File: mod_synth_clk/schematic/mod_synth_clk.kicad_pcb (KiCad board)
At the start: 2 copper layers, 17.8 x 113 mm, 9 parts, among them J1 Clock, J2 Conn_02x08_Odd_Even

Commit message: Shorten clock PCB to 109mm
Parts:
- moved J1 3.81 mm to (40.6, 128.3)
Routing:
- net Net-(J1-PadT): track 54.6 -> 50.8 mm
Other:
- board size 17.8 x 113 mm -> 17.8 x 109.2 mm
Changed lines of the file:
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@@
   )
   (module Connector_Audio:Jack_3.5mm_QingPu_WQP-PJ398SM_Vertical_CircularHoles (layer F.Cu)
-    (at 40.64 132.08 90)
+    (at 40.64 128.27 90)
     (descr "TRS 3.5mm, vertical, Thonkiconn, PCB mount, (http://www.qingpu-electronics.com/en/products/WQP-PJ398SM-362.html)")
     (tags "WQP-PJ398SM WQP-PJ301M-12 TRS 3.5mm mono vertical jack thonkiconn qingpu")
@@
     )
   )
+  (gr_line (start 55.88 134.62) (end 55.88 25.4) (layer Edge.Cuts) (width 0.05))
+  (gr_line (start 38.1 134.62) (end 55.88 134.62) (layer Edge.Cuts) (width 0.05))
+  (gr_line (start 38.1 25.4) (end 38.1 134.62) (layer Edge.Cuts) (width 0.05))
   (gr_line (start 55.88 25.4) (end 38.1 25.4) (layer Edge.Cuts) (width 0.05))
-  (gr_line (start 55.88 138.43) (end 55.88 25.4) (layer Edge.Cuts) (width 0.05))
-  (gr_line (start 38.1 138.43) (end 55.88 138.43) (layer Edge.Cuts) (width 0.05))
-  (gr_line (start 38.1 25.4) (end 38.1 138.43) (layer Edge.Cuts) (width 0.05))
   (segment (start 48.26 83.82) (end 48.26 85.09) (width 0.25) (layer F.Cu) (net 1))
   (segment (start 48.26 85.09) (end 52.07 85.09) (width 0.25) (layer F.Cu) (net 1))
@@
   (segment (start 50.8 54.61) (end 48.26 54.61) (width 0.25) (layer F.Cu) (net 32))
   (segment (start 48.26 54.61) (end 48.26 62.23) (width 0.25) (layer F.Cu) (net 32))
-  (segment (start 52.04 132.08) (end 52.04 90.2) (width 0.25) (layer F.Cu) (net 33))
-  (segment (start 52.04 90.2) (end 52.01 90.17) (width 0.25) (layer F.Cu) (net 33))
   (segment (start 52.01 90.17) (end 44.45 90.17) (width 0.25) (layer F.Cu) (net 33))
   (segment (start 44.45 90.17) (end 44.45 85.09) (width 0.25) (layer F.Cu) (net 33))
+  (segment (start 52.04 90.2) (end 52.04 128.27) (width 0.25) (layer F.Cu) (net 33))
+  (segment (start 52.01 90.17) (end 52.04 90.2) (width 0.25) (layer F.Cu) (net 33))
   (zone (net 5) (net_name GND) (layer B.Cu) (hatch edge 0.508)
     (connect_pads (clearance 0.508))
@@
     (polygon
       (pts
-        (xy 38.1 138.43) (xy 55.88 138.43) (xy 55.88 25.4) (xy 38.1 25.4)
+        (xy 55.88 134.62) (xy 38.1 134.62) (xy 38.1 25.4) (xy 55.88 25.4)
       )
     )

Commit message: Update PCB layouts
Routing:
- net Net-(J2-Pad3): track 0.00 -> 5.08 mm
- added copper zone on F.Cu, net GND
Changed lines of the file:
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@@
     (thickness 1.6)
     (drawings 4)
-    (tracks 49)
+    (tracks 51)
     (zones 0)
     (modules 9)
@@
   (segment (start 52.04 90.2) (end 52.04 128.27) (width 0.25) (layer F.Cu) (net 33))
   (segment (start 52.01 90.17) (end 52.04 90.2) (width 0.25) (layer F.Cu) (net 33))
+  (segment (start 45.72 109.22) (end 45.72 111.76) (width 0.25) (layer B.Cu) (net 40))
+  (segment (start 45.72 114.3) (end 45.72 111.76) (width 0.25) (layer B.Cu) (net 40))
+  (zone (net 5) (net_name GND) (layer F.Cu) (hatch edge 0.508)
+    (connect_pads (clearance 0.508))
+    (min_thickness 0.254)
+    (fill yes (arc_segments 32) (thermal_gap 0.508) (thermal_bridge_width 0.508))
+    (polygon
+      (pts
+        (xy 38.1 25.4) (xy 55.88 25.4) (xy 55.88 134.62) (xy 38.1 134.62)
+      )
+    )
+  )
   (zone (net 5) (net_name GND) (layer B.Cu) (hatch edge 0.508)
     (connect_pads (clearance 0.508))
@@
     (polygon
       (pts
-        (xy 55.88 134.62) (xy 38.1 134.62) (xy 38.1 25.4) (xy 55.88 25.4)
+        (xy 38.1 25.4) (xy 55.88 25.4) (xy 55.88 134.62) (xy 38.1 134.62)
       )
     )

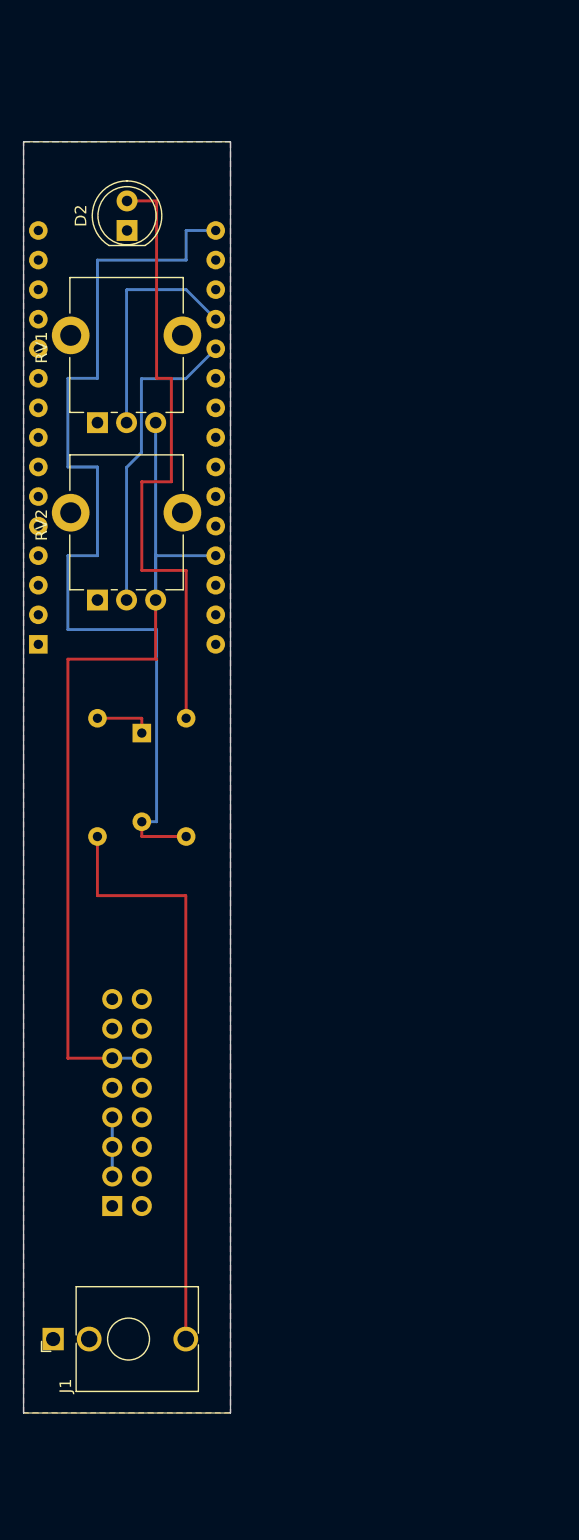
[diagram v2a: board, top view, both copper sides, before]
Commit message: Add possible PCB front panel
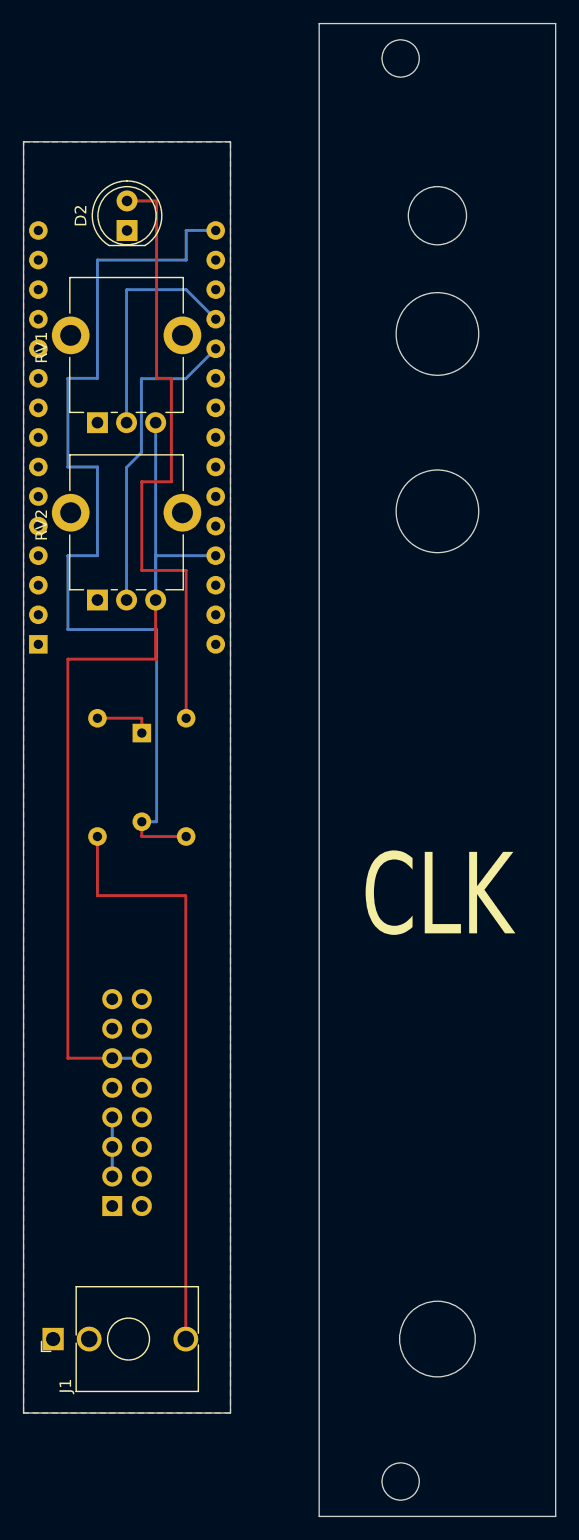
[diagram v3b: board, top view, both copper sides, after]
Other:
- board size 17.8 x 109.2 mm -> 45.7 x 128.3 mm
- board text added: "CLK"
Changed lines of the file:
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@@
   (general
     (thickness 1.6)
-    (drawings 4)
+    (drawings 15)
     (tracks 51)
     (zones 0)
@@
     )
   )
+  (gr_text CLK (at 73.66 90.17) (layer F.SilkS)
+    (effects (font (size 7 5) (thickness 1)))
+  )
+  (gr_circle (center 70.5 140.51) (end 72.1 140.51) (layer Edge.Cuts) (width 0.05))
+  (gr_circle (center 70.5 18.24) (end 72.1 18.24) (layer Edge.Cuts) (width 0.05))
+  (gr_circle (center 73.66 31.75) (end 76.16 31.75) (layer Edge.Cuts) (width 0.05))
+  (gr_circle (center 73.66 41.91) (end 77.21 41.91) (layer Edge.Cuts) (width 0.05))
+  (gr_circle (center 73.66 57.15) (end 77.21 57.15) (layer Edge.Cuts) (width 0.05))
+  (gr_circle (center 73.66 128.27) (end 76.91 128.27) (layer Edge.Cuts) (width 0.05))
+  (gr_line (start 83.82 15.24) (end 63.5 15.24) (layer Edge.Cuts) (width 0.05))
+  (gr_line (start 83.82 143.51) (end 83.82 15.24) (layer Edge.Cuts) (width 0.05))
+  (gr_line (start 63.5 143.51) (end 83.82 143.51) (layer Edge.Cuts) (width 0.05))
+  (gr_line (start 63.5 15.24) (end 63.5 143.51) (layer Edge.Cuts) (width 0.05))
   (gr_line (start 55.88 134.62) (end 55.88 25.4) (layer Edge.Cuts) (width 0.05))
   (gr_line (start 38.1 134.62) (end 55.88 134.62) (layer Edge.Cuts) (width 0.05))

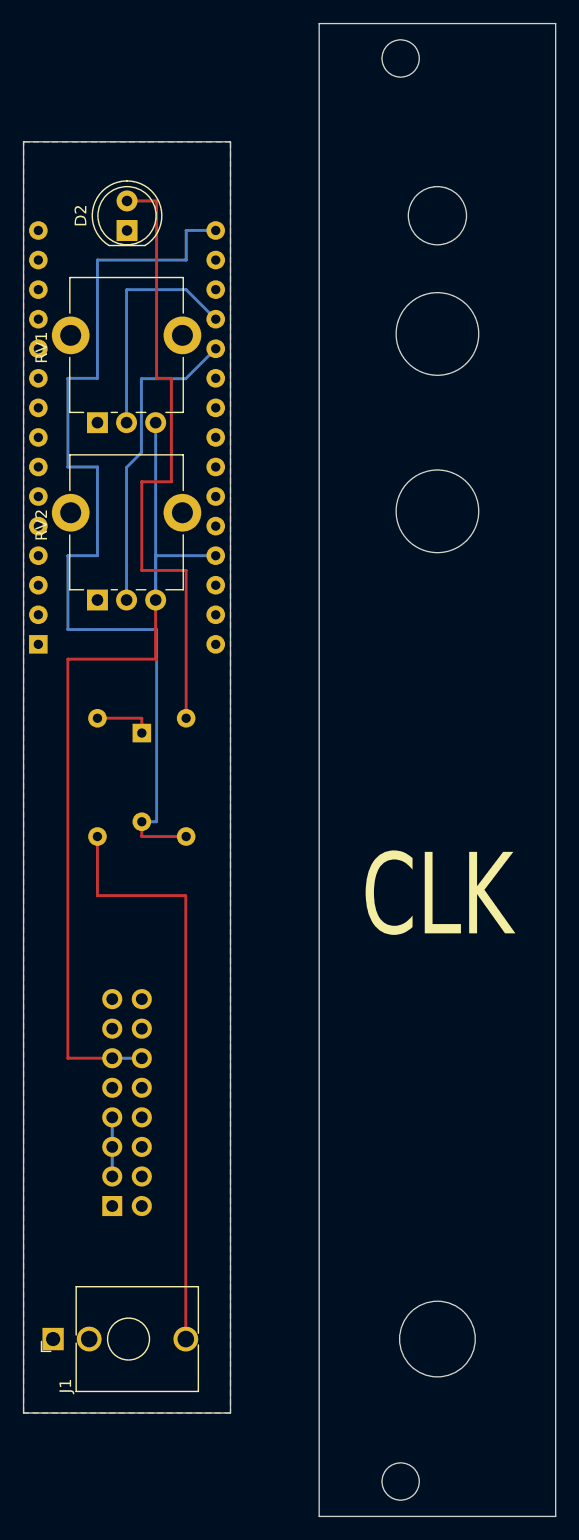
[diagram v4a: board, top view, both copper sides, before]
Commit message: Remove PCB front panel
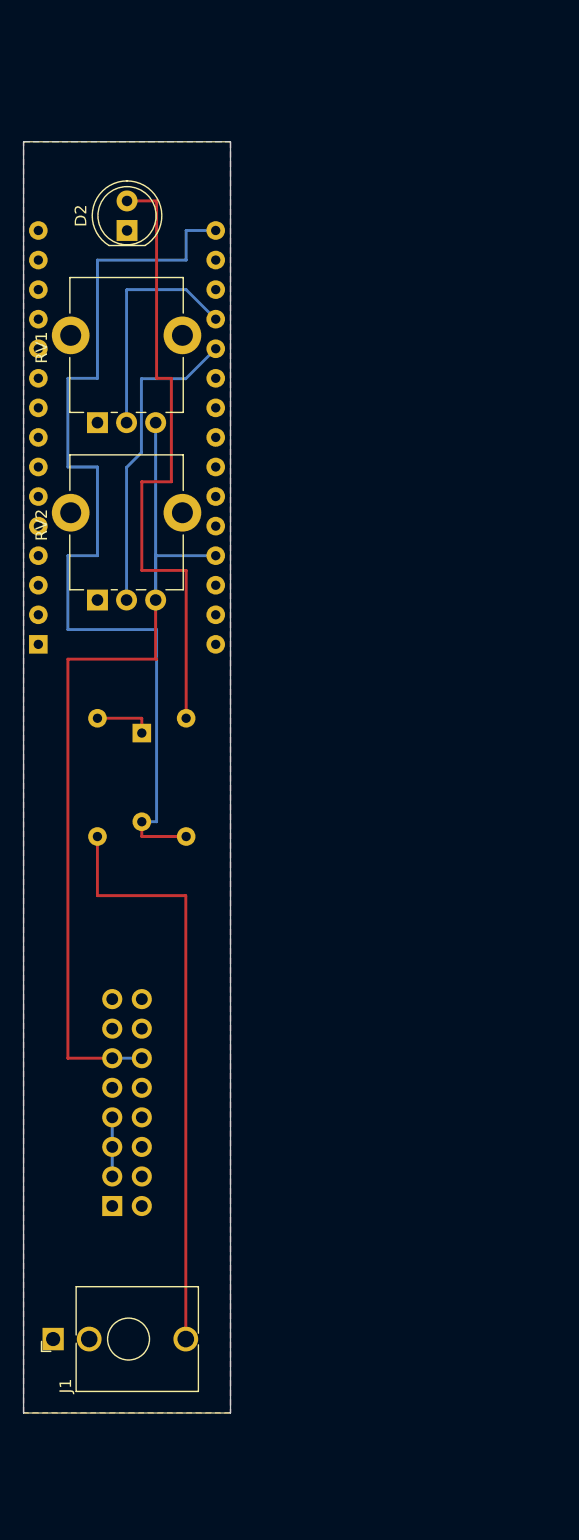
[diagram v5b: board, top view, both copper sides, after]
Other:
- board size 45.7 x 128.3 mm -> 17.8 x 109.2 mm
- board text removed: "CLK"
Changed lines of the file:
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@@
   (general
     (thickness 1.6)
-    (drawings 15)
+    (drawings 4)
     (tracks 51)
     (zones 0)
@@
     )
   )
-  (gr_text CLK (at 73.66 90.17) (layer F.SilkS)
-    (effects (font (size 7 5) (thickness 1)))
-  )
-  (gr_circle (center 70.5 140.51) (end 72.1 140.51) (layer Edge.Cuts) (width 0.05))
-  (gr_circle (center 70.5 18.24) (end 72.1 18.24) (layer Edge.Cuts) (width 0.05))
-  (gr_circle (center 73.66 31.75) (end 76.16 31.75) (layer Edge.Cuts) (width 0.05))
-  (gr_circle (center 73.66 41.91) (end 77.21 41.91) (layer Edge.Cuts) (width 0.05))
-  (gr_circle (center 73.66 57.15) (end 77.21 57.15) (layer Edge.Cuts) (width 0.05))
-  (gr_circle (center 73.66 128.27) (end 76.91 128.27) (layer Edge.Cuts) (width 0.05))
-  (gr_line (start 83.82 15.24) (end 63.5 15.24) (layer Edge.Cuts) (width 0.05))
-  (gr_line (start 83.82 143.51) (end 83.82 15.24) (layer Edge.Cuts) (width 0.05))
-  (gr_line (start 63.5 143.51) (end 83.82 143.51) (layer Edge.Cuts) (width 0.05))
-  (gr_line (start 63.5 15.24) (end 63.5 143.51) (layer Edge.Cuts) (width 0.05))
   (gr_line (start 55.88 134.62) (end 55.88 25.4) (layer Edge.Cuts) (width 0.05))
   (gr_line (start 38.1 134.62) (end 55.88 134.62) (layer Edge.Cuts) (width 0.05))
